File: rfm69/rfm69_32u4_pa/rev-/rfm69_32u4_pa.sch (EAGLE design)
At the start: 38 parts, among them K1 G5LE, SW1 SPST_TACT-KMR2, U1 433MHz, X2 USB_B_PTH, Y1 8MHz

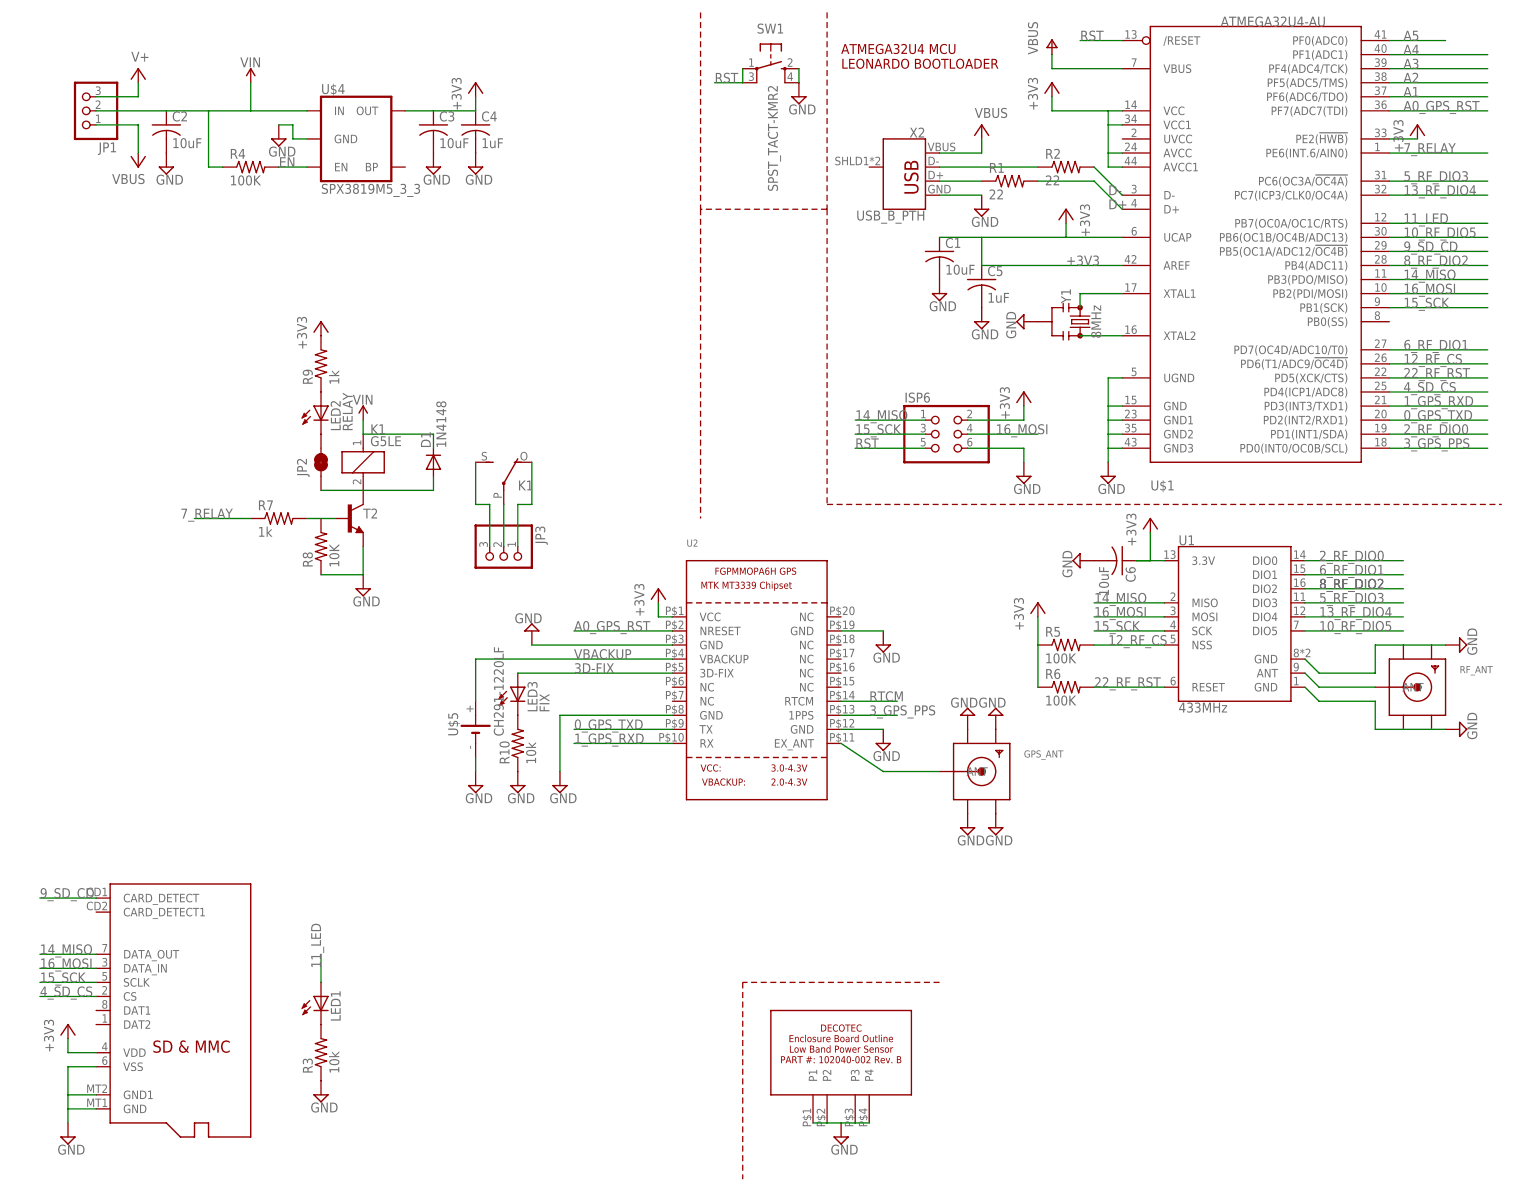
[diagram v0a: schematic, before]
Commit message: New project, RFM69 with Mitsubishi MOSFET PA and PGA103 LNA and associated switching.  incomplete, but mostly done.
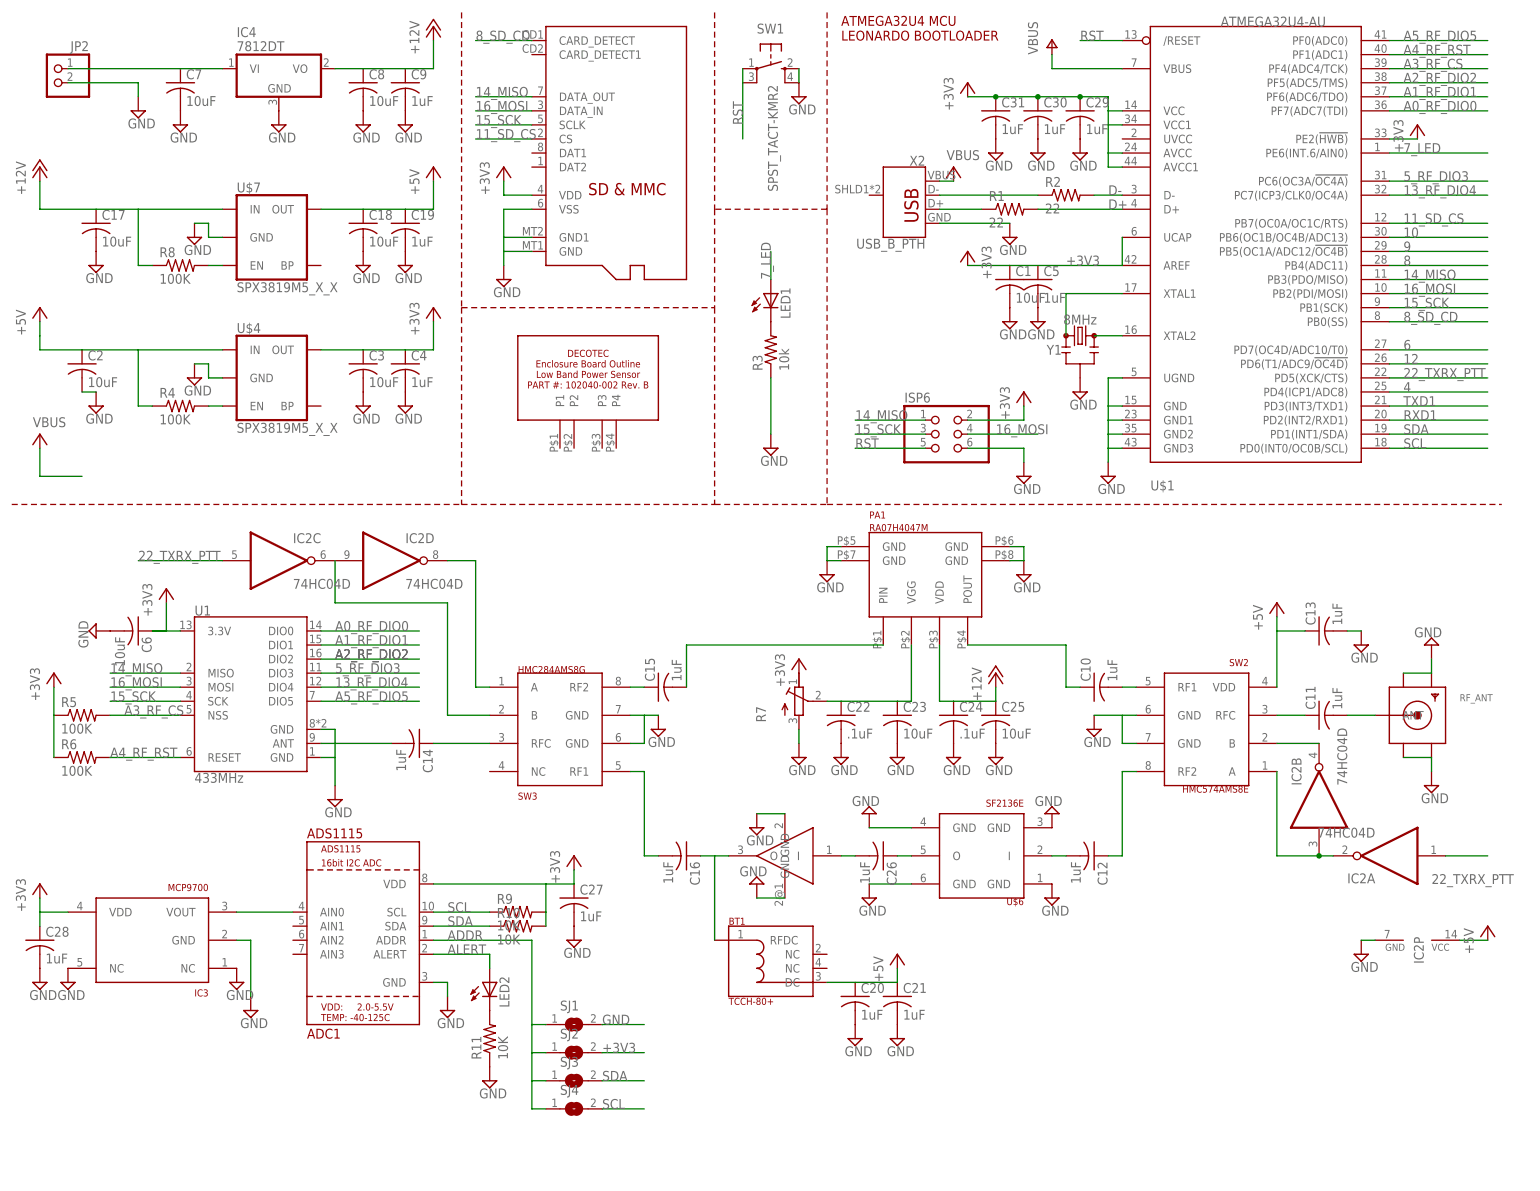
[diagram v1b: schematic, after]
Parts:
- removed D1: 1N4148, diode:DIODE-SOD323-R
- removed GPS_ANT: (no value), adafruit:SMACONNECTOR_EDGE
- removed JP1, JP3: (no value), pinhead:PINHD-1X3
- removed K1: G5LE, relay:G5LE
- removed LED3: FIX, adafruit:LEDCHIPLED_0805
- removed T2: (no value), transistor:MMBT2222ALT1-NPN-SOT23-BEC
- removed U2: (no value), adafruit:GPS_FGPMMOPA6H
- added ADC1: ADS1115, vtgs:ADS1115
- added BT1: TCCH-80+, kj4qlp:TCCH-80+
- added C10, C11, C12, C13, C14, C15, C16, C19, C20, C21, C26, C27, C28, C29, C30, C31, C9: 1uF, rcl:C-USC0805K
- added C17, C18, C23, C25, C7, C8: 10uF, rcl:C-USC0805K
- added C22, C24: .1uF, rcl:C-USC0805K
- added IC2: 74HC04D, 74xx-eu:74HC04D
- added IC3: MCP9700, vtgs:MCP9700
- added IC4: 7812DT, adafruit:7812DT
- added PA1: RA07H4047M, kj4qlp:RA07H4047M
- added R11: 10K, adafruit:R-US_R0805
- added SJ1, SJ2, SJ3, SJ4: (no value), jumper:SJ
- added SW2: HMC574AMS8E, kj4qlp:HMC574AMS8E
- added SW3: HMC284AMS8G, kj4qlp:HMC284AMS8G
- added U$6: SF2136E, kj4qlp:SF2136E
- added U$7: SPX3819M5_X_X, kj4qlp:V_REG_SPX3819-SOT23-5
- JP2: value JUMPER-SMT_2_NC_TRACE_SILK -> (none); device SparkFun-Jumpers:JUMPER-SMT_2_NC_TRACE_SILK -> pinhead:PINHD-1X2
- LED2: value RELAY -> (none)
- R10: value 10k -> 10K
- R7: value 1k -> (none); device adafruit:R-US_R0805 -> rcl:R-TRIMM3314G
- R8: value 10K -> 100K
- R9: value 1k -> 10K
- U$4: value SPX3819M5_3_3 -> SPX3819M5_X_X; device SparkFun-IC-Power:V_REG_SPX3819-SOT23-5 -> kj4qlp:V_REG_SPX3819-SOT23-5
- U$5: value CH291-1220LF -> PGA-103+; device battery:CH291-1220LF -> kj4qlp:PGA-103+
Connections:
- removed net 0_GPS_TXD: U$1.PD2(INT2/RXD1), U2.TX
- removed net 10_RF_DIO5: U$1.PB6(OC1B/OC4B/ADC13), U1.DIO5
- removed net 11_LED: LED1.A, U$1.PB7(OC0A/OC1C/RTS)
- removed net 12_RF_CS: R5.2, U$1.PD6(T1/ADC9/!OC4D), U1.NSS
- removed net 1_GPS_RXD: U$1.PD3(INT3/TXD1), U2.RX
- removed net 22_RF_RST: R6.2, U$1.PD5(XCK/CTS), U1.RESET
- removed net 2_RF_DIO0: U$1.PD1(INT1/SDA), U1.DIO0
- removed net 3D-FIX: LED3.A, U2.3D-FIX
- removed net 3_GPS_PPS: U$1.PD0(INT0/OC0B/SCL), U2.1PPS
- removed net 4_SD_CS: U$1.PD4(ICP1/ADC8), U$3.CS
- removed net 6_RF_DIO1: U$1.PD7(OC4D/ADC10/T0), U1.DIO1
- removed net 7_RELAY: R7.1, U$1.PE6(INT.6/AIN0)
- removed net 8_RF_DIO2: U$1.PB4(ADC11), U1.DIO2
- removed net 9_SD_CD: U$1.PB5(OC1A/ADC12/!OC4B), U$3.CARD_DETECT
- removed net A0_GPS_RST: U$1.PF7(ADC7(TDI), U2.NRESET
- removed net A1: U$1.PF6(ADC6/TDO)
- removed net A2: U$1.PF5(ADC5/TMS)
- removed net A3: U$1.PF4(ADC4/TCK)
- removed net A4: U$1.PF1(ADC1)
- removed net A5: U$1.PF0(ADC0)
- removed net RTCM: U2.RTCM
- removed net V+: JP1.3
- removed net VBACKUP: U$5.+, U2.VBACKUP
- removed net VIN: C2.1, D1.C, JP1.2, K11.1, R4.1, U$4.IN
- new net +12V: C17.1, C24.1, C25.1, C8.1, C9.1, IC4.VO, PA1.VDD, R8.1, U$7.IN
- new net +5V: BT1.DC, C13.1, C18.1, C19.1, C2.1, C20.1, C21.1, IC2P.VCC, R4.1, SW2.VDD, U$4.IN, U$7.OUT
- new net 10: U$1.PB6(OC1B/OC4B/ADC13)
- new net 11_SD_CS: U$1.PB7(OC0A/OC1C/RTS), U$3.CS
- new net 12: U$1.PD6(T1/ADC9/!OC4D)
- new net 22_TXRX_PTT: IC2A.I, IC2C.I, U$1.PD5(XCK/CTS)
- new net 4: U$1.PD4(ICP1/ADC8)
- new net 6: U$1.PD7(OC4D/ADC10/T0)
- new net 7_LED: LED1.A, U$1.PE6(INT.6/AIN0)
- new net 8: U$1.PB4(ADC11)
- new net 8_SD_CD: U$1.PB0(SS), U$3.CARD_DETECT
- new net 9: U$1.PB5(OC1A/ADC12/!OC4B)
- new net A0_RF_DIO0: U$1.PF7(ADC7(TDI), U1.DIO0
- new net A1_RF_DIO1: U$1.PF6(ADC6/TDO), U1.DIO1
- new net A2_RF_DIO2: U$1.PF5(ADC5/TMS), U1.DIO2
- new net A3_RF_CS: R5.2, U$1.PF4(ADC4/TCK), U1.NSS
- new net A4_RF_RST: R6.2, U$1.PF1(ADC1), U1.RESET
- new net A5_RF_DIO5: U$1.PF0(ADC0), U1.DIO5
- new net ADDR: ADC1.ADDR, SJ1.1, SJ2.1, SJ3.1, SJ4.1
- new net ALERT: ADC1.ALERT, LED2.A
- new net N$11: C11.2, RF_ANT.ANT
- new net N$15: C16.2, SW3.RF1
- new net N$16: IC2D.O, SW3.A
- new net N$17: BT1.RFDC, C16.1, U$5.O
- new net N$18: C22.1, C23.1, PA1.VGG, R7.S
- new net N$19: C12.1, SW2.RF2
- new net N$20: C12.2, U$6.I
- new net N$21: IC2C.O, IC2D.I, SW3.B
- new net N$22: C26.2, U$5.I
- new net N$23: R8.2, U$7.EN
- new net N$24: LED2.C, R11.2
- new net N$6: C10.1, PA1.POUT
- new net RXD1: U$1.PD2(INT2/RXD1)
- new net SCL: ADC1.SCL, R9.1, SJ4.2, U$1.PD0(INT0/OC0B/SCL)
- new net SDA: ADC1.SDA, R10.1, SJ3.2, U$1.PD1(INT1/SDA)
- new net TXD1: U$1.PD3(INT3/TXD1)
- new net V_PA_TEMP: ADC1.AIN0, IC3.VOUT
- net +3V3: now also ADC1.VDD, C27.1, C28.1, C29.1, C30.1, C31.1, IC3.VDD, R10.2, R7.E, SJ2.2; no longer U2.VCC
- net ANT: now also C14.2; no longer RF_ANT.ANT
- net GND: now also ADC1.GND, C13.2, C17.2, C18.2, C19.2, C20.2, C21.2, C22.2, C23.2, C24.2, C25.2, C27.2, C28.2, C29.2, C30.2, C31.2, C7.2, C8.2, C9.2, IC2P.GND, IC3.GND, IC3.NC@1, IC3.NC@5, IC4.GND, JP2.2, PA1.GND@1, PA1.GND@2, PA1.GND@3, PA1.GND@4, R11.1, R7.A, SJ1.2, SW2.GND@1, SW2.GND@2, SW3.GND@1, SW3.GND@2, U$5.GND@1, U$5.GND@2, U$6.GND@1, U$6.GND@3, U$6.GND@4, U$6.GND@6, U$7.GND; no longer GPS_ANT.GND1, GPS_ANT.GND2, GPS_ANT.GND3, GPS_ANT.GND4, R10.1, R8.1, T2.E, U$2.P1, U$2.P2, U$2.P3, U$2.P4, U$5.-, U2.GND@1, U2.GND@2, U2.GND@3, U2.GND@4
- net N$10: now also C26.1, U$6.O; no longer JP2.2, LED2.C
- net N$12: now also C11.1, SW2.RFC; no longer JP3.2, K12.P
- net N$13: now also C14.1, SW3.RFC; no longer JP3.1, K12.O
- net N$14: now also C15.1, SW3.RF2; no longer JP3.3, K12.S
- net N$4: now also C15.2, PA1.PIN; no longer D1.A, JP2.1, K11.2, T2.C
- net N$5: now also C7.1, IC4.VI, JP2.1; no longer LED3.C, R10.2
- net N$7: now also C10.2, SW2.RF1; no longer GPS_ANT.ANT, U2.EX_ANT
- net N$8: now also IC2A.O, IC2B.I, SW2.A; no longer R7.2, R8.2, T2.B
- net N$9: now also IC2B.O, SW2.B; no longer LED2.A, R9.1
- net VBUS: no longer JP1.1
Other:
- moved on the sheet: C1, C2, C3, C4, C5, C6, LED1, LED2, R1, R10, R2, R3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

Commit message: lots of detail updates, including test point additions, need to clean up silk screen.....
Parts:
- added D1: MBR120, adafruit:DIODESOD-123
- added SJ5: (no value), jumper:SJ2W
- added TP-1, TP-10, TP-11, TP-12, TP-2, TP-3, TP-4, TP-5, TP-6, TP-7, TP-8, TP-9, TP1, TP10, TP11, TP12, TP13, TP14, TP15, TP2, TP3, TP4, TP5, TP6, TP7, TP8, TP9: TPSQTP10SQ, testpad:TPSQTP10SQ
- C20: value 1uF -> 0.33uF
- C21: value 1uF -> 10uF
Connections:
- new net 5V_VREG: C18.1, C19.1, SJ5.3, U$7.OUT
- new net N$25: ADC1.AIN1, TP1.TP
- new net N$26: ADC1.AIN2, TP2.TP
- new net N$27: ADC1.AIN3, TP3.TP
- net +3V3: now also TP11.TP, TP14.TP, TP5.TP
- net +5V: now also D1.C, SJ5.2, TP10.TP, TP15.TP; no longer C18.1, C19.1, U$7.OUT
- net 10: now also TP-10.TP
- net 12: now also TP8.TP
- net 13_RF_DIO4: now also TP-5.TP
- net 22_TXRX_PTT: now also TP-12.TP
- net 4: now also TP9.TP
- net 5_RF_DIO3: now also TP-4.TP
- net 6: now also TP7.TP
- net 8: now also TP-8.TP
- net 9: now also TP-9.TP
- net A0_RF_DIO0: now also TP-1.TP
- net A1_RF_DIO1: now also TP-2.TP
- net A2_RF_DIO2: now also TP-3.TP
- net A5_RF_DIO5: now also TP-6.TP
- net GND: now also TP12.TP, TP13.TP, TP4.TP, TP6.TP, U$2.P1, U$2.P2, U$2.P3, U$2.P4
- net RXD1: now also TP-11.TP
- net TXD1: now also TP-7.TP
- net VBUS: now also D1.A, SJ5.1
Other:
- moved on the sheet: ADC1, BT1, C10, C11, C12, C13, C14, C15, C16, C2, C20, C21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

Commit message: Final version of Rev- board including Gerbers and Osh Park pictures.  This is the version sent to Osh PArk for fab.
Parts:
- removed IC4: 7812DT, adafruit:7812DT
- removed JP2: (no value), pinhead:PINHD-1X2
- removed SW3: HMC284AMS8G, kj4qlp:HMC284AMS8G
- removed TP9: TPSQTP10SQ, testpad:TPSQTP10SQ
- removed U$4, U$7: SPX3819M5_X_X, kj4qlp:V_REG_SPX3819-SOT23-5
- added AIN0, AIN1, AIN2, AIN3, DIO3, DIO5, PTT, PTT1, PTT2, SW1A, SW1B, SW2A, SW2B, VGG: TPSQTP10SQ, testpad:TPSQTP10SQ
- added BTN1: SPST_TACT-KMR2, adafruit:SPST_TACT-KMR2
- added F1: 500mA, adafruit:PTCFUSE-1206
- added GND, VIN: (no value), pinhead:PINHD-1X1
- added PTT-HI, PTT-LO, PWR: (no value), adafruit:LEDCHIPLED_0805
- added R12, R13, R18: 10K, adafruit:R-US_R0805
- added R14, R15, R16, R17: 100, adafruit:R-US_R0805
- added TVS1: ESD8472, kj4qlp:ESD8472
- added VR1: 7812DT, adafruit:7812DT
- added VR2, VR3: SPX3819M5_X_X, kj4qlp:V_REG_SPX3819-SOT23-5
- C10, C11, C12, C15, C16, C26: value 1uF -> .01uF
- R3: value 10k -> 10K
- SW1: value SPST_TACT-KMR2 -> HMC284AMS8G; device adafruit:SPST_TACT-KMR2 -> kj4qlp:HMC284AMS8G
- TP3, TP7: value TPSQTP10SQ -> TPSQTP20SQ; device testpad:TPSQTP10SQ -> testpad:TPSQTP20SQ
- renumbered LED2 to LED-ALT, TP-1 to DIO0, TP-11 to RXD1, TP-2 to DIO1, TP-3 to DIO2, TP-5 to DIO4, TP-7 to TXD1, TP13 to GND@1, U$1 to IC1, U$5 to PGA-103+, U1 to RF1, X2 to USB
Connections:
- new net AIN1: ADC1.AIN1, AIN1.TP
- new net AIN2: ADC1.AIN2, AIN2.TP
- new net AIN3: ADC1.AIN3, AIN3.TP
- new net SW1A: IC2D.O, R15.2, SW1A.TP
- new net SW1B: IC2C.O, IC2D.I, R14.2, SW1B.TP
- new net SW2A: IC2A.O, IC2B.I, R17.1, SW2A.TP
- new net SW2B: IC2B.O, R16.1, SW2B.TP
- new net VIN: C7.1, TP3.TP, VIN.1, VR1.VI
- new net VUSB: F1.1, USB.VBUS
- net +12V: now also VR1.VO, VR2.IN; no longer IC4.VO, U$7.IN
- net +3V3: now also PWR.A, R18.1, TP2.TP, VR3.OUT; no longer U$4.OUT
- net +5V: now also VR3.IN; no longer U$4.IN
- net 12: now also TP-12.TP; no longer TP8.TP
- net 22_TXRX_PTT: now also PTT.TP, PTT2.TP; no longer TP-12.TP
- net 4: now also TP-4.TP; no longer TP9.TP
- net 5V_VREG: now also VR2.OUT; no longer U$7.OUT
- net 5_RF_DIO3: now also DIO3.TP; no longer TP-4.TP
- net 6: now also TP-6.TP; no longer TP7.TP
- net A5_RF_DIO5: now also DIO5.TP; no longer TP-6.TP
- net EN: now also VR3.EN; no longer U$4.EN
- net GND: now also BTN1.S, BTN1.S1, GND.1, R12.1, R13.1, SW1.GND@1, SW1.GND@2, TP1.TP, TP7.TP, TP8.TP, TVS1.P$2, VR1.GND, VR2.GND, VR3.GND; no longer IC4.GND, JP2.2, SW1.S, SW1.S1, SW3.GND@1, SW3.GND@2, U$2.P1, U$2.P2, U$2.P3, U$2.P4, U$4.GND, U$7.GND
- net N$11: now also TVS1.P$1
- net N$13: now also SW1.RFC; no longer SW3.RFC
- net N$14: now also SW1.RF2; no longer SW3.RF2
- net N$15: now also SW1.RF1; no longer SW3.RF1
- net N$16: now also R14.1, SW1.B; no longer IC2D.O, SW3.A
- net N$18: now also VGG.TP
- net N$21: now also R15.1, SW1.A; no longer IC2C.O, IC2D.I, SW3.B
- net N$23: now also VR2.EN; no longer U$7.EN
- net N$25: now also R17.2, SW2.A; no longer ADC1.AIN1, TP1.TP
- net N$26: now also R16.2, SW2.B; no longer ADC1.AIN2, TP2.TP
- net N$27: now also PTT-LO.A, R18.2; no longer ADC1.AIN3, TP3.TP
- net N$5: now also PTT-HI.A, PTT-LO.C, PTT1.TP; no longer C7.1, IC4.VI, JP2.1
- net N$8: now also PTT-HI.C, R12.2; no longer IC2A.O, IC2B.I, SW2.A
- net N$9: now also PWR.C, R13.2; no longer IC2B.O, SW2.B
- net RST: now also BTN1.P, BTN1.P1; no longer SW1.P, SW1.P1
- net VBUS: now also F1.2; no longer USB.VBUS
- net V_PA_TEMP: now also AIN0.TP
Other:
- moved on the sheet: C1, C11, C13, C17, C18, C19, C2, C28, C3, C4, C5, C7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
